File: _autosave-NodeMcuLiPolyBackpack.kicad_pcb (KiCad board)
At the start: 2 copper layers, 15.2 x 26.7 mm, 14 parts, among them P1 Switch, P2 G BAT, P3 Battery, P4 G 5V, U1 MCP73831

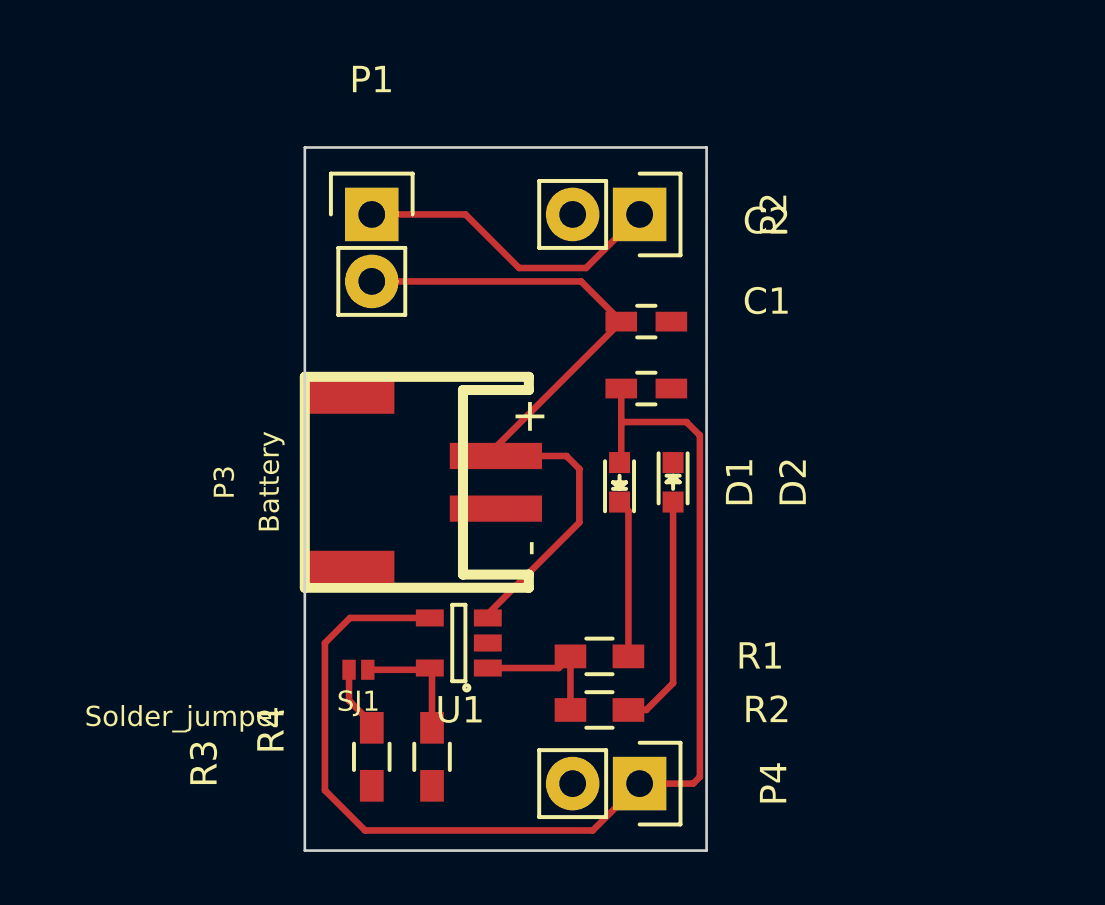
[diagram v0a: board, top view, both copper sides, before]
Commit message: Revision de Medidas de pines
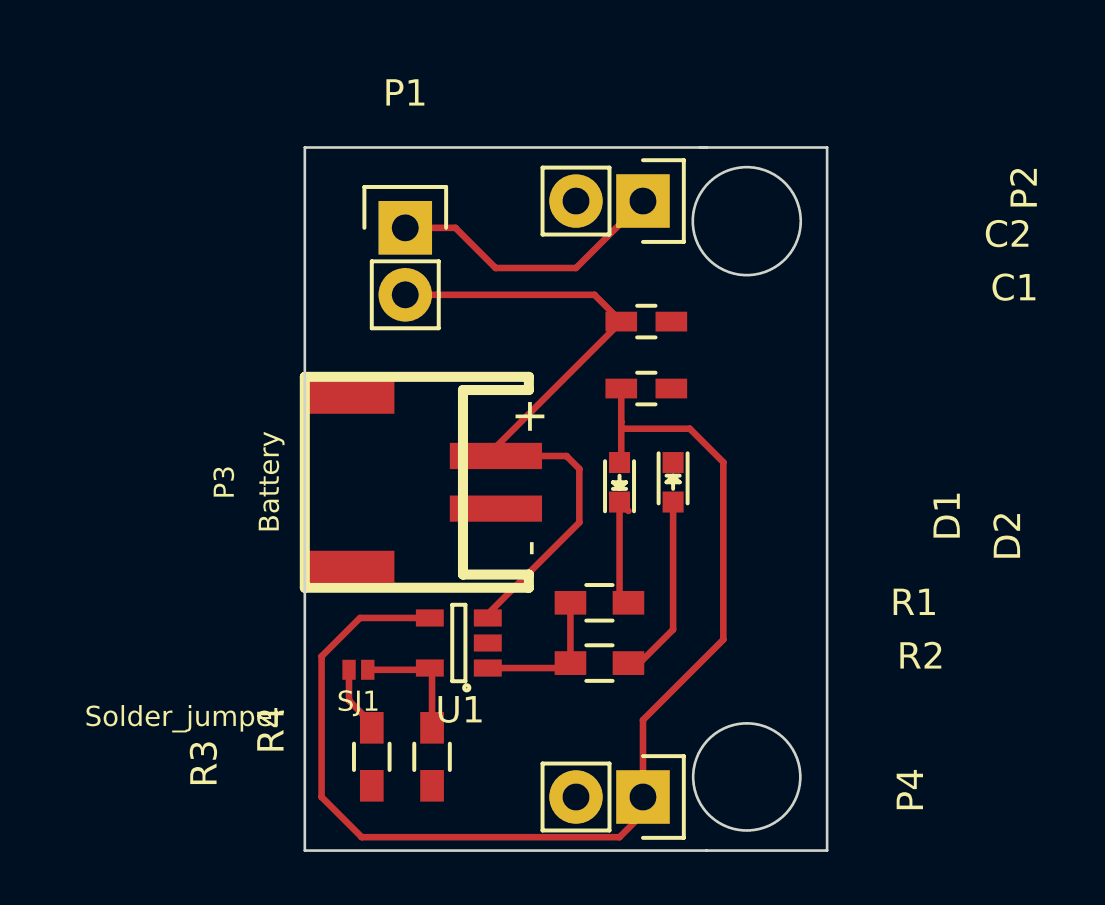
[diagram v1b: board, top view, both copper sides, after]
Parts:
- moved R1 2.03 mm to (138.2, 112.5)
- moved R2 1.78 mm to (138.2, 114.8)
- moved P1 1.37 mm to (130.8, 98.3)
- moved P2 0.52 mm to (139.8, 97.3)
- moved P4 0.52 mm to (139.8, 119.9)
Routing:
- net Net-(D2-Pad2): track 8.99 -> 7.06 mm
- net Net-(D1-Pad1): track 5.99 -> 4.44 mm
- net /VBat: track 27.6 -> 26.1 mm
- net Net-(P1-Pad1): track 11.8 -> 10.7 mm
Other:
- board size 15.2 x 26.7 mm -> 19.8 x 26.7 mm
